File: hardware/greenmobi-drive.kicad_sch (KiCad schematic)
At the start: 36 parts, among them J101 UBAT, J102 GND, J103 Encoder/Hall, J104 Motor NTC, J107 ADC, J108 ADC, U101 BMI323

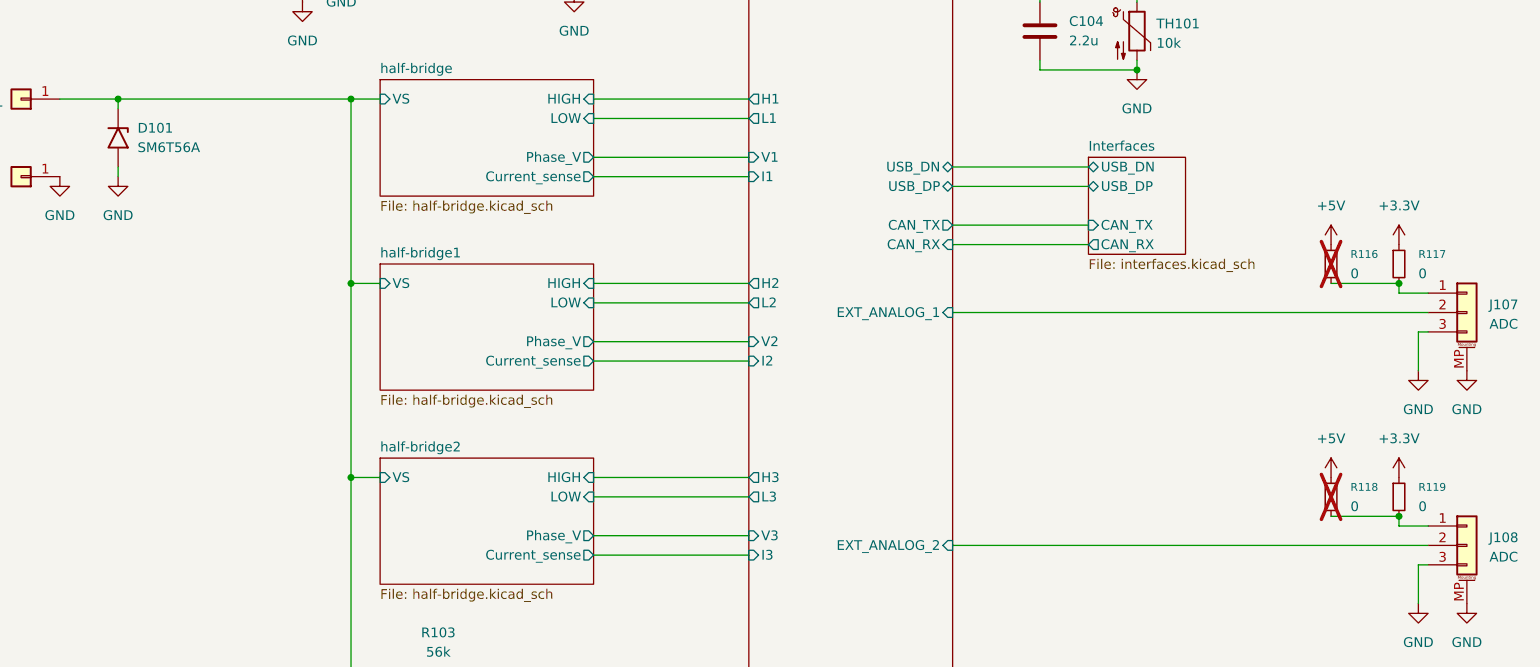
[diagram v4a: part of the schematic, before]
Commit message: Changed bootstrap resistor to 0 Ohm
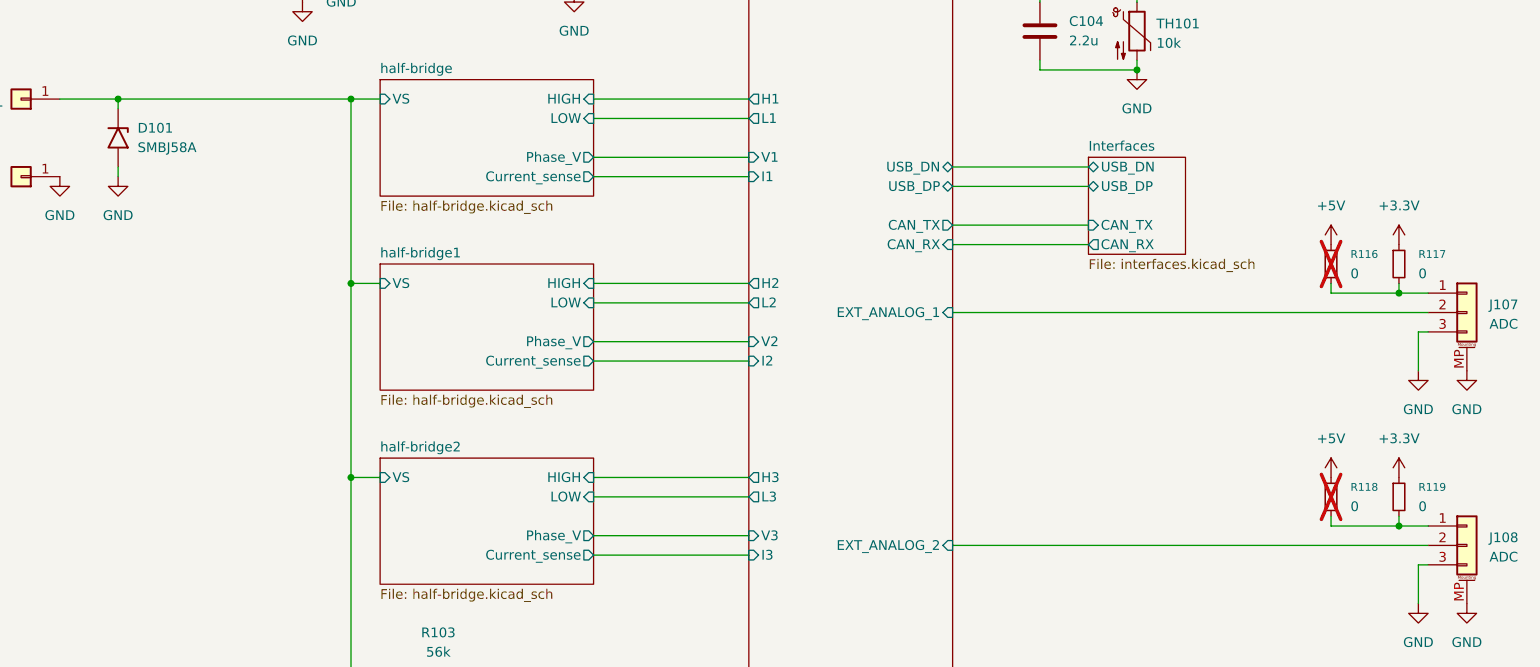
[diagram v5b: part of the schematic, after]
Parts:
- D101: value SM6T56A -> SMBJ58A
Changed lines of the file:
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@@
 	)
 	(junction
-		(at 234.95 133.35)
+		(at 111.76 39.37)
 		(diameter 0)
 		(color 0 0 0 0)
 	)
 	(junction
-		(at 111.76 39.37)
+		(at 200.66 74.93)
 		(diameter 0)
 		(color 0 0 0 0)
 	)
 	(junction
-		(at 200.66 74.93)
+		(at 234.95 104.14)
 		(diameter 0)
 		(color 0 0 0 0)
@@
 	)
 	(junction
-		(at 40.64 33.02)
+		(at 234.95 134.62)
 		(diameter 0)
 		(color 0 0 0 0)
 	)
 	(junction
-		(at 127 58.42)
+		(at 40.64 33.02)
 		(diameter 0)
 		(color 0 0 0 0)
 	)
 	(junction
-		(at 40.64 55.88)
+		(at 127 58.42)
 		(diameter 0)
 		(color 0 0 0 0)
 	)
 	(junction
-		(at 111.76 29.21)
+		(at 40.64 55.88)
 		(diameter 0)
 		(color 0 0 0 0)
 	)
 	(junction
-		(at 234.95 102.87)
+		(at 111.76 29.21)
 		(diameter 0)
 		(color 0 0 0 0)
@@
 	(wire
 		(pts
+			(xy 226.06 104.14) (xy 226.06 102.87)
+		)
+		(stroke
+			(width 0)
+			(type default)
+		)
+	)
+	(wire
+		(pts
 			(xy 102.87 29.21) (xy 111.76 29.21)
 		)
@@
 	(wire
 		(pts
-			(xy 234.95 104.14) (xy 234.95 102.87)
+			(xy 59.69 78.74) (xy 67.31 78.74)
 		)
 		(stroke
@@
 	(wire
 		(pts
-			(xy 59.69 78.74) (xy 67.31 78.74)
+			(xy 176.53 27.94) (xy 180.34 27.94)
 		)
 		(stroke
@@
 	(wire
 		(pts
-			(xy 176.53 27.94) (xy 180.34 27.94)
+			(xy 176.53 137.16) (xy 238.76 137.16)
 		)
 		(stroke
@@
 	(wire
 		(pts
-			(xy 176.53 137.16) (xy 238.76 137.16)
+			(xy 97.79 29.21) (xy 102.87 29.21)
 		)
 		(stroke
@@
 	(wire
 		(pts
-			(xy 97.79 29.21) (xy 102.87 29.21)
+			(xy 226.06 104.14) (xy 234.95 104.14)
 		)
 		(stroke
@@
 	(wire
 		(pts
-			(xy 226.06 102.87) (xy 234.95 102.87)
+			(xy 54.61 55.88) (xy 40.64 55.88)
 		)
 		(stroke
@@
 	(wire
 		(pts
-			(xy 54.61 55.88) (xy 40.64 55.88)
+			(xy 195.58 40.64) (xy 195.58 39.37)
 		)
 		(stroke
@@
 	(wire
 		(pts
-			(xy 195.58 40.64) (xy 195.58 39.37)
+			(xy 185.42 27.94) (xy 186.69 27.94)
 		)
 		(stroke
@@
 	(wire
 		(pts
-			(xy 185.42 27.94) (xy 186.69 27.94)
+			(xy 234.95 104.14) (xy 234.95 102.87)
 		)
 		(stroke
@@
 	(wire
 		(pts
-			(xy 226.06 133.35) (xy 234.95 133.35)
+			(xy 226.06 134.62) (xy 234.95 134.62)
 		)
 		(stroke
@@
 	(wire
 		(pts
+			(xy 226.06 134.62) (xy 226.06 133.35)
+		)
+		(stroke
+			(width 0)
+			(type default)
+		)
+	)
+	(wire
+		(pts
 			(xy 111.76 35.56) (xy 111.76 39.37)
 		)
@@
 			)
 		)
-		(property "Value" "SM6T56A"
+		(property "Value" "SMBJ58A"
 			(at 69.85 85.0899 90)
 			(effects

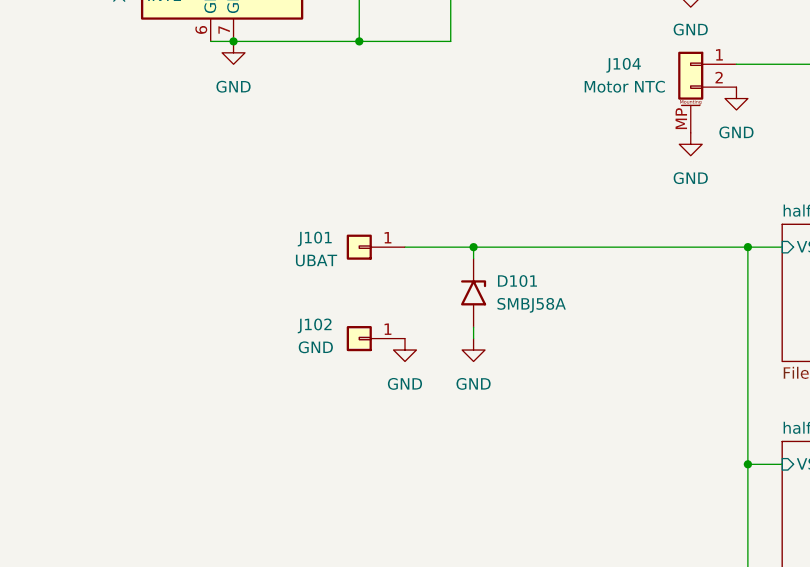
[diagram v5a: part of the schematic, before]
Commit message: Reduce board size
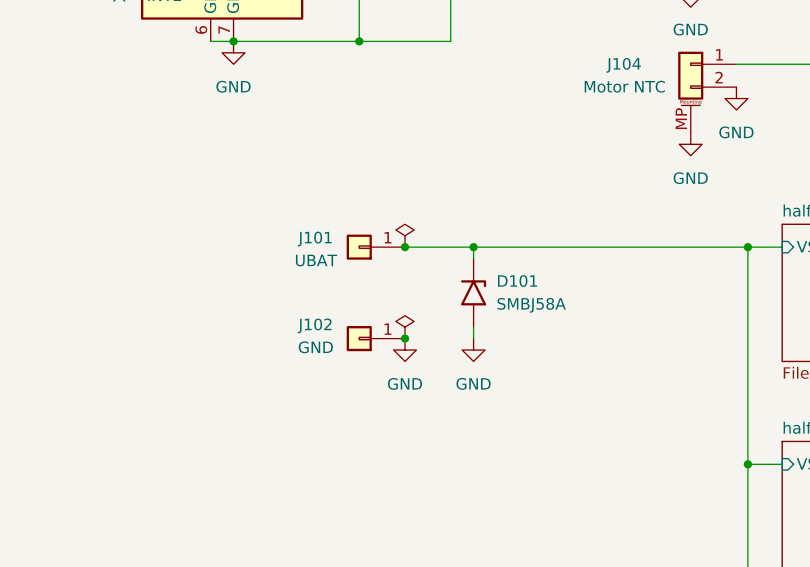
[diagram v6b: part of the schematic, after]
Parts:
- J101, J102: footprint Connector_Wire:SolderWirePad_1x01_SMD_4x8mm -> MountingHole:MountingHole_3.2mm_M3_ISO14580_Pad_TopBottom
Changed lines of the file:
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@@
 	)
 	(junction
+		(at 59.69 88.9)
+		(diameter 0)
+		(color 0 0 0 0)
+	)
+	(junction
 		(at 97.79 78.74)
 		(diameter 0)
@@
 	)
 	(junction
+		(at 59.69 78.74)
+		(diameter 0)
+		(color 0 0 0 0)
+	)
+	(junction
 		(at 97.79 102.87)
 		(diameter 0)
@@
 	)
 	(symbol
+		(lib_id "power:PWR_FLAG")
+		(at 59.69 78.74 0)
+		(unit 1)
+		(exclude_from_sim no)
+		(in_bom yes)
+		(on_board yes)
+		(dnp no)
+		(fields_autoplaced yes)
+		(property "Reference" "#FLG0102"
+			(at 59.69 76.835 0)
+			(effects
+				(font
+					(size 1.27 1.27)
+				)
+				(hide yes)
+			)
+		)
+		(property "Value" "PWR_FLAG"
+			(at 59.69 73.66 0)
+			(effects
+				(font
+					(size 1.27 1.27)
+				)
+				(hide yes)
+			)
+		)
+		(property "Footprint" ""
+			(at 59.69 78.74 0)
+			(effects
+				(font
+					(size 1.27 1.27)
+				)
+				(hide yes)
+			)
+		)
+		(property "Datasheet" "~"
+			(at 59.69 78.74 0)
+			(effects
+				(font
+					(size 1.27 1.27)
+				)
+				(hide yes)
+			)
+		)
+		(property "Description" "Special symbol for telling ERC where power comes from"
+			(at 59.69 78.74 0)
+			(effects
+				(font
+					(size 1.27 1.27)
+				)
+				(hide yes)
+			)
+		)
+		(pin "1"
+		)
+		(instances
+			(project "greenmobi-drive"
+				(path "/a12b77e7-bd0f-4a70-9ba2-19a87ce48819"
+					(reference "#FLG0102")
+					(unit 1)
+				)
+			)
+		)
+	)
+	(symbol
 		(lib_id "Device:C_Small")
 		(at 127 62.23 0)
@@
 			)
 		)
-		(property "Footprint" "Connector_Wire:SolderWirePad_1x01_SMD_4x8mm"
+		(property "Footprint" "MountingHole:MountingHole_3.2mm_M3_ISO14580_Pad_TopBottom"
 			(at 54.61 88.9 0)
 			(effects
@@
 			)
 		)
-		(property "Footprint" "Connector_Wire:SolderWirePad_1x01_SMD_4x8mm"
+		(property "Footprint" "MountingHole:MountingHole_3.2mm_M3_ISO14580_Pad_TopBottom"
 			(at 54.61 78.74 0)
 			(effects
@@
 					(unit 1)
 				)
+			)
+		)
+	)
+	(symbol
+		(lib_id "power:PWR_FLAG")
+		(at 59.69 88.9 0)
+		(unit 1)
+		(exclude_from_sim no)
+		(in_bom yes)
+		(on_board yes)
+		(dnp no)
+		(fields_autoplaced yes)
+		(property "Reference" "#FLG0101"
+			(at 59.69 86.995 0)
+			(effects
+				(font
+					(size 1.27 1.27)
+				)
+				(hide yes)
+			)
+		)
+		(property "Value" "PWR_FLAG"
+			(at 59.69 83.82 0)
+			(effects
+				(font
+					(size 1.27 1.27)
+				)
+				(hide yes)
+			)
+		)
+		(property "Footprint" ""
+			(at 59.69 88.9 0)
+			(effects
+				(font
+					(size 1.27 1.27)
+				)
+				(hide yes)
+			)
+		)
+		(property "Datasheet" "~"
+			(at 59.69 88.9 0)
+			(effects
+				(font
+					(size 1.27 1.27)
+				)
+				(hide yes)
+			)
+		)
+		(property "Description" "Special symbol for telling ERC where power comes from"
+			(at 59.69 88.9 0)
+			(effects
+				(font
+					(size 1.27 1.27)
+				)
+				(hide yes)
+			)
+		)
+		(pin "1"
+		)
+		(instances
+			(project ""
+				(path "/a12b77e7-bd0f-4a70-9ba2-19a87ce48819"
+					(reference "#FLG0101")
+					(unit 1)
+				)

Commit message: Changed bootstrap diode and gate resistor
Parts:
- J103: footprint Connector_JST:JST_GH_SM05B-GHS-TB_1x05-1MP_P1.25mm_Horizontal -> Connector_JST:JST_PH_S5B-PH-SM4-TB_1x05-1MP_P2.00mm_Horizontal
- J104: footprint Connector_JST:JST_GH_SM02B-GHS-TB_1x02-1MP_P1.25mm_Horizontal -> Connector_JST:JST_PH_S2B-PH-SM4-TB_1x02-1MP_P2.00mm_Horizontal
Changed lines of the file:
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@@
 			)
 		)
-		(property "Footprint" "Connector_JST:JST_GH_SM02B-GHS-TB_1x02-1MP_P1.25mm_Horizontal"
+		(property "Footprint" "Connector_JST:JST_PH_S2B-PH-SM4-TB_1x02-1MP_P2.00mm_Horizontal"
 			(at 91.44 58.42 0)
 			(effects
@@
 			)
 		)
-		(property "Footprint" "Connector_JST:JST_GH_SM05B-GHS-TB_1x05-1MP_P1.25mm_Horizontal"
+		(property "Footprint" "Connector_JST:JST_PH_S5B-PH-SM4-TB_1x05-1MP_P2.00mm_Horizontal"
 			(at 91.44 39.37 0)
 			(effects

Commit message: Layout work
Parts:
- J103: footprint Connector_JST:JST_PH_S5B-PH-SM4-TB_1x05-1MP_P2.00mm_Horizontal -> Connector_JST:JST_PH_B5B-PH-SM4-TB_1x05-1MP_P2.00mm_Vertical
- J104: footprint Connector_JST:JST_PH_S2B-PH-SM4-TB_1x02-1MP_P2.00mm_Horizontal -> Connector_JST:JST_PH_B2B-PH-SM4-TB_1x02-1MP_P2.00mm_Vertical
- J107, J108: footprint Connector_JST:JST_GH_SM03B-GHS-TB_1x03-1MP_P1.25mm_Horizontal -> Connector_JST:JST_PH_B3B-PH-SM4-TB_1x03-1MP_P2.00mm_Vertical
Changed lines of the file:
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@@
 			)
 		)
-		(property "Footprint" "Connector_JST:JST_GH_SM03B-GHS-TB_1x03-1MP_P1.25mm_Horizontal"
+		(property "Footprint" "Connector_JST:JST_PH_B3B-PH-SM4-TB_1x03-1MP_P2.00mm_Vertical"
 			(at 243.84 137.16 0)
 			(effects
@@
 			)
 		)
-		(property "Footprint" "Connector_JST:JST_PH_S2B-PH-SM4-TB_1x02-1MP_P2.00mm_Horizontal"
+		(property "Footprint" "Connector_JST:JST_PH_B2B-PH-SM4-TB_1x02-1MP_P2.00mm_Vertical"
 			(at 91.44 58.42 0)
 			(effects
@@
 			)
 		)
-		(property "Footprint" "Connector_JST:JST_PH_S5B-PH-SM4-TB_1x05-1MP_P2.00mm_Horizontal"
+		(property "Footprint" "Connector_JST:JST_PH_B5B-PH-SM4-TB_1x05-1MP_P2.00mm_Vertical"
 			(at 91.44 39.37 0)
 			(effects
@@
 			)
 		)
-		(property "Footprint" "Connector_JST:JST_GH_SM03B-GHS-TB_1x03-1MP_P1.25mm_Horizontal"
+		(property "Footprint" "Connector_JST:JST_PH_B3B-PH-SM4-TB_1x03-1MP_P2.00mm_Vertical"
 			(at 243.84 106.68 0)
 			(effects
